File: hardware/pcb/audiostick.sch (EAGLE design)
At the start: 61 parts, among them IC1 TPS73633MBDV, IC3 PCM5102ASW, IC5 AP22804W5, IC6 TINY13V-10SSU, J1 AVRISP6TH127, J2 AUDIO_JACK_3.5MM_PTH, J3 USB-B, T1 BC850

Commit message: Rationalised BOM a little
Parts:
- C14: value 2u2 -> 4u7; device rcl:C-EUC0805 -> rcl:C-EUC0603
- C17: value 1u -> 2u2
- C3: value 10u -> 4u7
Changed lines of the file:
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@@
 <grid distance="0.1" unitdist="inch" unit="inch" style="lines" multiple="1" display="no" altdistance="0.01" altunitdist="inch" altunit="inch"/>
 <layers>
-<layer number="1" name="Top" color="4" fill="1" visible="yes" active="no"/>
-<layer number="16" name="Bottom" color="1" fill="1" visible="yes" active="no"/>
-<layer number="17" name="Pads" color="2" fill="1" visible="yes" active="no"/>
-<layer number="18" name="Vias" color="2" fill="1" visible="yes" active="no"/>
-<layer number="19" name="Unrouted" color="6" fill="1" visible="yes" active="no"/>
-<layer number="20" name="Dimension" color="24" fill="1" visible="yes" active="no"/>
-<layer number="21" name="tPlace" color="7" fill="1" visible="yes" active="no"/>
-<layer number="22" name="bPlace" color="7" fill="1" visible="yes" active="no"/>
-<layer number="23" name="tOrigins" color="15" fill="1" visible="yes" active="no"/>
-<layer number="24" name="bOrigins" color="15" fill="1" visible="yes" active="no"/>
-<layer number="25" name="tNames" color="7" fill="1" visible="yes" active="no"/>
-<layer number="26" name="bNames" color="7" fill="1" visible="yes" active="no"/>
-<layer number="27" name="tValues" color="7" fill="1" visible="yes" active="no"/>
-<layer number="28" name="bValues" color="7" fill="1" visible="yes" active="no"/>
+<layer number="1" name="Top" color="4" fill="1" visible="no" active="no"/>
+<layer number="16" name="Bottom" color="1" fill="1" visible="no" active="no"/>
+<layer number="17" name="Pads" color="2" fill="1" visible="no" active="no"/>
+<layer number="18" name="Vias" color="2" fill="1" visible="no" active="no"/>
+<layer number="19" name="Unrouted" color="6" fill="1" visible="no" active="no"/>
+<layer number="20" name="Dimension" color="24" fill="1" visible="no" active="no"/>
+<layer number="21" name="tPlace" color="7" fill="1" visible="no" active="no"/>
+<layer number="22" name="bPlace" color="7" fill="1" visible="no" active="no"/>
+<layer number="23" name="tOrigins" color="15" fill="1" visible="no" active="no"/>
+<layer number="24" name="bOrigins" color="15" fill="1" visible="no" active="no"/>
+<layer number="25" name="tNames" color="7" fill="1" visible="no" active="no"/>
+<layer number="26" name="bNames" color="7" fill="1" visible="no" active="no"/>
+<layer number="27" name="tValues" color="7" fill="1" visible="no" active="no"/>
+<layer number="28" name="bValues" color="7" fill="1" visible="no" active="no"/>
 <layer number="29" name="tStop" color="7" fill="3" visible="no" active="no"/>
 <layer number="30" name="bStop" color="7" fill="6" visible="no" active="no"/>
@@
 <layer number="35" name="tGlue" color="7" fill="4" visible="no" active="no"/>
 <layer number="36" name="bGlue" color="7" fill="5" visible="no" active="no"/>
-<layer number="37" name="tTest" color="7" fill="1" visible="yes" active="no"/>
-<layer number="38" name="bTest" color="7" fill="1" visible="yes" active="no"/>
+<layer number="37" name="tTest" color="7" fill="1" visible="no" active="no"/>
+<layer number="38" name="bTest" color="7" fill="1" visible="no" active="no"/>
 <layer number="39" name="tKeepout" color="4" fill="11" visible="no" active="no"/>
 <layer number="40" name="bKeepout" color="1" fill="11" visible="no" active="no"/>
@@
 <layer number="44" name="Drills" color="7" fill="1" visible="no" active="no"/>
 <layer number="45" name="Holes" color="7" fill="1" visible="no" active="no"/>
-<layer number="46" name="Milling" color="3" fill="1" visible="yes" active="no"/>
-<layer number="47" name="Measures" color="7" fill="1" visible="yes" active="no"/>
-<layer number="48" name="Document" color="7" fill="1" visible="yes" active="no"/>
-<layer number="49" name="Reference" color="7" fill="1" visible="yes" active="no"/>
-<layer number="50" name="dxf" color="7" fill="1" visible="yes" active="no"/>
-<layer number="51" name="tDocu" color="7" fill="1" visible="yes" active="no"/>
-<layer number="52" name="bDocu" color="7" fill="1" visible="yes" active="no"/>
-<layer number="53" name="tGND_GNDA" color="7" fill="9" visible="yes" active="no"/>
-<layer number="54" name="bGND_GNDA" color="1" fill="9" visible="yes" active="no"/>
-<layer number="56" name="wert" color="7" fill="1" visible="yes" active="no"/>
-<layer number="57" name="tCAD" color="7" fill="1" visible="yes" active="no"/>
-<layer number="59" name="tCarbon" color="7" fill="1" visible="yes" active="no"/>
-<layer number="60" name="bCarbon" color="7" fill="1" visible="yes" active="no"/>
+<layer number="46" name="Milling" color="3" fill="1" visible="no" active="no"/>
+<layer number="47" name="Measures" color="7" fill="1" visible="no" active="no"/>
+<layer number="48" name="Document" color="7" fill="1" visible="no" active="no"/>
+<layer number="49" name="Reference" color="7" fill="1" visible="no" active="no"/>
+<layer number="50" name="dxf" color="7" fill="1" visible="no" active="no"/>
+<layer number="51" name="tDocu" color="7" fill="1" visible="no" active="no"/>
+<layer number="52" name="bDocu" color="7" fill="1" visible="no" active="no"/>
+<layer number="53" name="tGND_GNDA" color="7" fill="9" visible="no" active="no"/>
+<layer number="54" name="bGND_GNDA" color="1" fill="9" visible="no" active="no"/>
+<layer number="56" name="wert" color="7" fill="1" visible="no" active="no"/>
+<layer number="57" name="tCAD" color="7" fill="1" visible="no" active="no"/>
+<layer number="59" name="tCarbon" color="7" fill="1" visible="no" active="no"/>
+<layer number="60" name="bCarbon" color="7" fill="1" visible="no" active="no"/>
 <layer number="88" name="SimResults" color="9" fill="1" visible="yes" active="yes"/>
 <layer number="89" name="SimProbes" color="9" fill="1" visible="yes" active="yes"/>
@@
 <part name="SUPPLY2" library="supply2" library_urn="urn:adsk.eagle:library:372" deviceset="+5V/1" device=""/>
 <part name="IC5" library="AudioStick" deviceset="AP22804" device="W5" package3d_urn="urn:adsk.eagle:package:6644359/2"/>
-<part name="C17" library="rcl" library_urn="urn:adsk.eagle:library:334" deviceset="C-EU" device="C0603" package3d_urn="urn:adsk.eagle:package:23616/2" value="1u"/>
+<part name="C17" library="rcl" library_urn="urn:adsk.eagle:library:334" deviceset="C-EU" device="C0603" package3d_urn="urn:adsk.eagle:package:23616/2" value="2u2"/>
 <part name="C19" library="rcl" library_urn="urn:adsk.eagle:library:334" deviceset="C-EU" device="C0603" package3d_urn="urn:adsk.eagle:package:23616/2" value="100n"/>
 <part name="GND23" library="supply1" library_urn="urn:adsk.eagle:library:371" deviceset="GND" device=""/>
@@
 <part name="D3" library="AudioStick" deviceset="TVS-1" device="" package3d_urn="urn:adsk.eagle:package:23555/3"/>
 <part name="GND31" library="supply1" library_urn="urn:adsk.eagle:library:371" deviceset="GND" device=""/>
-<part name="C14" library="rcl" library_urn="urn:adsk.eagle:library:334" deviceset="C-EU" device="C0805" package3d_urn="urn:adsk.eagle:package:23617/2" value="2u2"/>
+<part name="C14" library="rcl" library_urn="urn:adsk.eagle:library:334" deviceset="C-EU" device="C0603" package3d_urn="urn:adsk.eagle:package:23616/2" value="4u7"/>
 <part name="GND32" library="supply1" library_urn="urn:adsk.eagle:library:371" deviceset="GND" device=""/>
 <part name="GND25" library="supply1" library_urn="urn:adsk.eagle:library:371" deviceset="GND" device=""/>
 <part name="GND14" library="supply1" library_urn="urn:adsk.eagle:library:371" deviceset="GND" device=""/>
 <part name="L3" library="rcl" library_urn="urn:adsk.eagle:library:334" deviceset="R-EU_" device="R0603" package3d_urn="urn:adsk.eagle:package:23555/3" value="F"/>
-<part name="C3" library="rcl" library_urn="urn:adsk.eagle:library:334" deviceset="C-EU" device="C0603" package3d_urn="urn:adsk.eagle:package:23616/2" value="10u"/>
+<part name="C3" library="rcl" library_urn="urn:adsk.eagle:library:334" deviceset="C-EU" device="C0603" package3d_urn="urn:adsk.eagle:package:23616/2" value="4u7"/>
 <part name="IC1" library="AudioStick" deviceset="TPS73633" device="MBDV" package3d_urn="urn:adsk.eagle:package:6644359/2"/>
 <part name="C16" library="rcl" library_urn="urn:adsk.eagle:library:334" deviceset="C-EU" device="C0603" package3d_urn="urn:adsk.eagle:package:23616/2" value="10n"/>

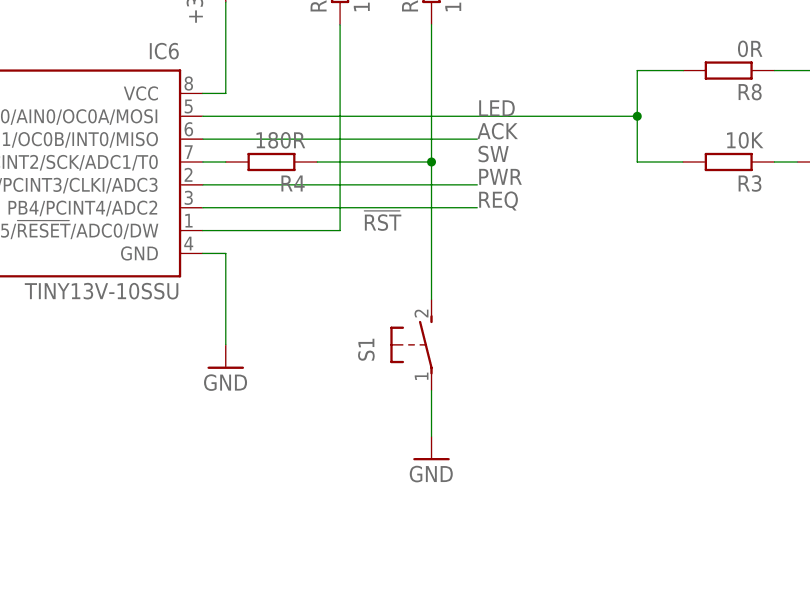
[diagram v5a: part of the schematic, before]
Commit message: Revert to EVQ switch
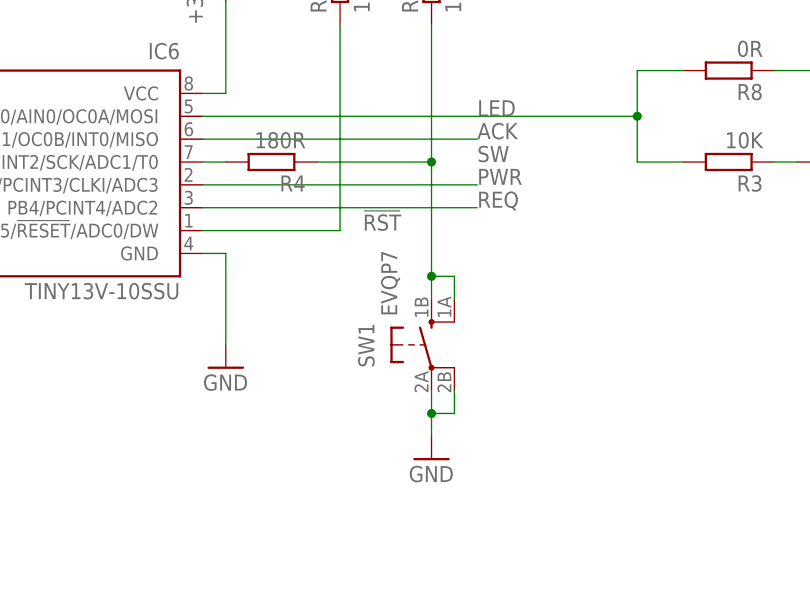
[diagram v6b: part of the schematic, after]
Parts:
- removed S1: (no value), switch-omron:31-XX
- added SW1: EVQP7, AudioStick:EVQP7
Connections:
- net GND: now also SW1.P, SW1.P1; no longer S1.P
- net SW: now also SW1.S, SW1.S1; no longer S1.S
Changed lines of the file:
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@@
 <part name="R4" library="rcl" library_urn="urn:adsk.eagle:library:334" deviceset="R-EU_" device="R0603" package3d_urn="urn:adsk.eagle:package:23555/3" value="180R"/>
 <part name="R8" library="rcl" library_urn="urn:adsk.eagle:library:334" deviceset="R-EU_" device="R0603" package3d_urn="urn:adsk.eagle:package:23555/3" value="0R"/>
-<part name="S1" library="switch-omron" library_urn="urn:adsk.eagle:library:377" deviceset="31-XX" device="" package3d_urn="urn:adsk.eagle:package:27487/1"/>
+<part name="SW1" library="AudioStick" deviceset="EVQP7" device=""/>
 </parts>
 <sheets>
@@
 <attribute name="VALUE" x="120.65" y="356.362" size="1.778" layer="96" rot="R180"/>
 </instance>
-<instance part="S1" gate="1" x="83.82" y="322.58" smashed="yes">
-<attribute name="NAME" x="77.47" y="320.675" size="1.778" layer="95" rot="R90"/>
+<instance part="SW1" gate="G$1" x="83.82" y="322.58" smashed="yes">
+<attribute name="NAME" x="77.47" y="320.04" size="1.778" layer="95" rot="R90"/>
 <attribute name="VALUE" x="80.01" y="325.755" size="1.778" layer="96" rot="R90"/>
 </instance>
@@
 <segment>
 <pinref part="GND1" gate="1" pin="GND"/>
-<wire x1="83.82" y1="312.42" x2="83.82" y2="317.5" width="0.1524" layer="91"/>
-<pinref part="S1" gate="1" pin="P"/>
+<wire x1="83.82" y1="312.42" x2="83.82" y2="314.96" width="0.1524" layer="91"/>
+<pinref part="SW1" gate="G$1" pin="P"/>
+<pinref part="SW1" gate="G$1" pin="P1"/>
+<wire x1="83.82" y1="314.96" x2="83.82" y2="317.5" width="0.1524" layer="91"/>
+<wire x1="83.82" y1="314.96" x2="86.36" y2="314.96" width="0.1524" layer="91"/>
+<wire x1="86.36" y1="314.96" x2="86.36" y2="317.5" width="0.1524" layer="91"/>
+<junction x="83.82" y="314.96"/>
 </segment>
 <segment>
@@
 <segment>
 <pinref part="R9" gate="G$1" pin="1"/>
-<wire x1="83.82" y1="327.66" x2="83.82" y2="342.9" width="0.1524" layer="91"/>
+<wire x1="83.82" y1="327.66" x2="83.82" y2="330.2" width="0.1524" layer="91"/>
+<wire x1="83.82" y1="330.2" x2="83.82" y2="342.9" width="0.1524" layer="91"/>
 <wire x1="83.82" y1="342.9" x2="83.82" y2="358.14" width="0.1524" layer="91"/>
 <label x="88.9" y="342.9" size="1.778" layer="95"/>
@@
 <wire x1="71.12" y1="342.9" x2="83.82" y2="342.9" width="0.1524" layer="91"/>
 <junction x="83.82" y="342.9"/>
-<pinref part="S1" gate="1" pin="S"/>
-</segment>
-<segment>
+<pinref part="SW1" gate="G$1" pin="S"/>
+<pinref part="SW1" gate="G$1" pin="S1"/>
+<wire x1="83.82" y1="330.2" x2="86.36" y2="330.2" width="0.1524" layer="91"/>
+<wire x1="86.36" y1="330.2" x2="86.36" y2="327.66" width="0.1524" layer="91"/>
+<junction x="83.82" y="330.2"/>
+</segment>
+<segment>

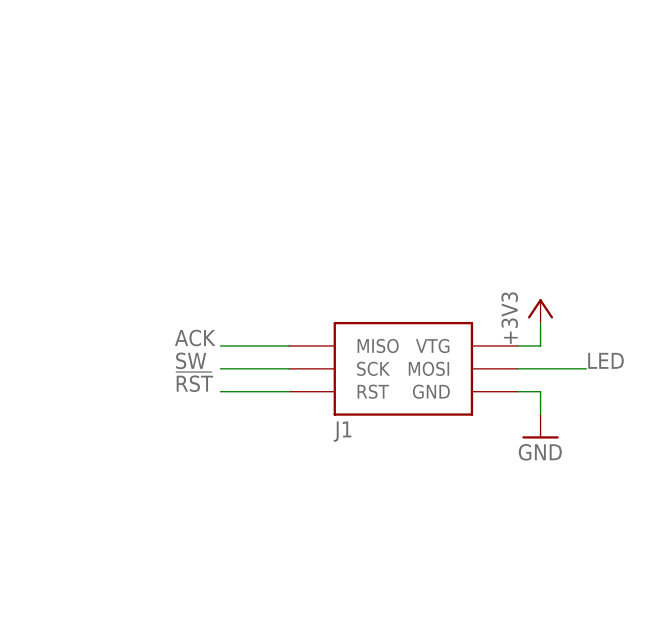
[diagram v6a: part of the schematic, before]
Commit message: Update board, BOM, and firmware
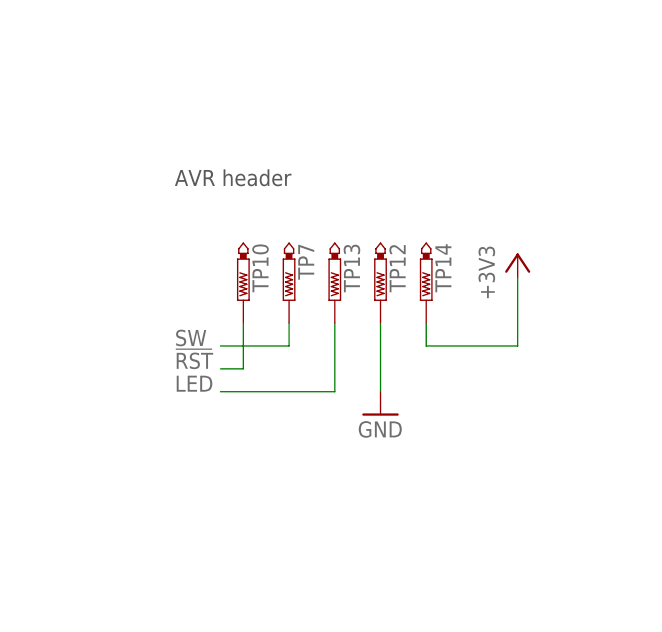
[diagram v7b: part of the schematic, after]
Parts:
- removed J1: AVRISP6TH127, AWJLEagleLib:AVRISP6TH127
- added TP10, TP12, TP13, TP14, TP7: PTR1TP08R, testpad:PTR1TP08R
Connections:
- net !RST: now also TP10.TP; no longer J1.RST
- net +3V3: now also TP14.TP; no longer J1.VTG
- net ACK: no longer J1.MISO
- net GND: now also TP12.TP; no longer J1.GND
- net LED: now also TP13.TP; no longer J1.MOSI
- net SW: now also TP7.TP; no longer J1.SCK
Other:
- note added: "AVR header"
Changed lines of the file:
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@@
 <part name="R13" library="rcl" library_urn="urn:adsk.eagle:library:334" deviceset="R-EU_" device="R0603" package3d_urn="urn:adsk.eagle:package:23555/3" value="10K"/>
 <part name="IC6" library="atmel" library_urn="urn:adsk.eagle:library:105" deviceset="TINY13" device="SSU" package3d_urn="urn:adsk.eagle:package:4358/1" technology="V-10"/>
-<part name="J1" library="AWJLEagleLib" deviceset="AVRISP6" device="TH127"/>
 <part name="+3V5" library="supply1" library_urn="urn:adsk.eagle:library:371" deviceset="+3V3" device=""/>
 <part name="GND19" library="supply1" library_urn="urn:adsk.eagle:library:371" deviceset="GND" device=""/>
@@
 <part name="R8" library="rcl" library_urn="urn:adsk.eagle:library:334" deviceset="R-EU_" device="R0603" package3d_urn="urn:adsk.eagle:package:23555/3" value="0R"/>
 <part name="SW1" library="AudioStick" deviceset="EVQP7" device=""/>
+<part name="TP7" library="testpad" library_urn="urn:adsk.eagle:library:385" deviceset="PTR1" device="TP08R" package3d_urn="urn:adsk.eagle:package:27956/1" value="PTR1TP08R"/>
+<part name="TP10" library="testpad" library_urn="urn:adsk.eagle:library:385" deviceset="PTR1" device="TP08R" package3d_urn="urn:adsk.eagle:package:27956/1" value="PTR1TP08R"/>
+<part name="TP12" library="testpad" library_urn="urn:adsk.eagle:library:385" deviceset="PTR1" device="TP08R" package3d_urn="urn:adsk.eagle:package:27956/1" value="PTR1TP08R"/>
+<part name="TP13" library="testpad" library_urn="urn:adsk.eagle:library:385" deviceset="PTR1" device="TP08R" package3d_urn="urn:adsk.eagle:package:27956/1" value="PTR1TP08R"/>
+<part name="TP14" library="testpad" library_urn="urn:adsk.eagle:library:385" deviceset="PTR1" device="TP08R" package3d_urn="urn:adsk.eagle:package:27956/1" value="PTR1TP08R"/>
 </parts>
 <sheets>
@@
 <text x="119.38" y="96.52" size="1.778" layer="97">ATtiny13 supply</text>
 <text x="134.62" y="358.14" size="1.778" layer="97">Kingbright KPA-3010</text>
+<text x="200.66" y="360.68" size="1.778" layer="97">AVR header</text>
 </plain>
 <instances>
@@
 <attribute name="VALUE" x="55.88" y="327.66" size="1.778" layer="96" rot="MR0"/>
 </instance>
-<instance part="J1" gate="G$1" x="226.06" y="340.36" smashed="yes">
-<attribute name="NAME" x="218.44" y="332.74" size="1.778" layer="95"/>
-</instance>
-<instance part="+3V5" gate="G$1" x="241.3" y="347.98" smashed="yes">
-<attribute name="VALUE" x="238.76" y="342.9" size="1.778" layer="96" rot="R90"/>
-</instance>
-<instance part="GND19" gate="1" x="241.3" y="332.74" smashed="yes">
-<attribute name="VALUE" x="238.76" y="330.2" size="1.778" layer="96"/>
+<instance part="+3V5" gate="G$1" x="238.76" y="353.06" smashed="yes">
+<attribute name="VALUE" x="236.22" y="347.98" size="1.778" layer="96" rot="R90"/>
+</instance>
+<instance part="GND19" gate="1" x="223.52" y="335.28" smashed="yes">
+<attribute name="VALUE" x="220.98" y="332.74" size="1.778" layer="96"/>
 </instance>
 <instance part="TP1" gate="G$1" x="147.32" y="88.9" smashed="yes" rot="R90">
@@
 <attribute name="NAME" x="77.47" y="320.04" size="1.778" layer="95" rot="R90"/>
 <attribute name="VALUE" x="80.01" y="325.755" size="1.778" layer="96" rot="R90"/>
+</instance>
+<instance part="TP7" gate="G$1" x="213.36" y="347.98" smashed="yes" rot="R180">
+<attribute name="NAME" x="214.376" y="354.33" size="1.778" layer="95" rot="R270"/>
+<attribute name="TP_SIGNAL_NAME" x="212.09" y="350.52" size="1.778" layer="97" rot="R180"/>
+</instance>
+<instance part="TP10" gate="G$1" x="208.28" y="347.98" smashed="yes" rot="R180">
+<attribute name="NAME" x="209.296" y="354.33" size="1.778" layer="95" rot="R270"/>
+<attribute name="TP_SIGNAL_NAME" x="207.01" y="350.52" size="1.778" layer="97" rot="R180"/>
+</instance>
+<instance part="TP12" gate="G$1" x="223.52" y="347.98" smashed="yes" rot="R180">
+<attribute name="NAME" x="224.536" y="354.33" size="1.778" layer="95" rot="R270"/>
+<attribute name="TP_SIGNAL_NAME" x="222.25" y="350.52" size="1.778" layer="97" rot="R180"/>
+</instance>
+<instance part="TP13" gate="G$1" x="218.44" y="347.98" smashed="yes" rot="R180">
+<attribute name="NAME" x="219.456" y="354.33" size="1.778" layer="95" rot="R270"/>
+<attribute name="TP_SIGNAL_NAME" x="217.17" y="350.52" size="1.778" layer="97" rot="R180"/>
+</instance>
+<instance part="TP14" gate="G$1" x="228.6" y="347.98" smashed="yes" rot="R180">
+<attribute name="NAME" x="229.616" y="354.33" size="1.778" layer="95" rot="R270"/>
+<attribute name="TP_SIGNAL_NAME" x="227.33" y="350.52" size="1.778" layer="97" rot="R180"/>
 </instance>
 </instances>
@@
 </segment>
 <segment>
-<pinref part="J1" gate="G$1" pin="GND"/>
 <pinref part="GND19" gate="1" pin="GND"/>
-<wire x1="238.76" y1="337.82" x2="241.3" y2="337.82" width="0.1524" layer="91"/>
-<wire x1="241.3" y1="337.82" x2="241.3" y2="335.28" width="0.1524" layer="91"/>
+<pinref part="TP12" gate="G$1" pin="TP"/>
+<wire x1="223.52" y1="337.82" x2="223.52" y2="345.44" width="0.1524" layer="91"/>
 </segment>
 <segment>
@@
 </segment>
 <segment>
-<pinref part="J1" gate="G$1" pin="VTG"/>
 <pinref part="+3V5" gate="G$1" pin="+3V3"/>
-<wire x1="238.76" y1="342.9" x2="241.3" y2="342.9" width="0.1524" layer="91"/>
-<wire x1="241.3" y1="342.9" x2="241.3" y2="345.44" width="0.1524" layer="91"/>
+<wire x1="228.6" y1="342.9" x2="238.76" y2="342.9" width="0.1524" layer="91"/>
+<wire x1="238.76" y1="342.9" x2="238.76" y2="350.52" width="0.1524" layer="91"/>
+<pinref part="TP14" gate="G$1" pin="TP"/>
+<wire x1="228.6" y1="345.44" x2="228.6" y2="342.9" width="0.1524" layer="91"/>
 </segment>
 <segment>
@@
 <net name="!RST" class="0">
 <segment>
-<pinref part="J1" gate="G$1" pin="RST"/>
-<wire x1="213.36" y1="337.82" x2="205.74" y2="337.82" width="0.1524" layer="91"/>
-<label x="200.66" y="337.82" size="1.778" layer="95"/>
+<label x="200.66" y="340.36" size="1.778" layer="95"/>
+<pinref part="TP10" gate="G$1" pin="TP"/>
+<wire x1="208.28" y1="340.36" x2="205.74" y2="340.36" width="0.1524" layer="91"/>
+<wire x1="208.28" y1="345.44" x2="208.28" y2="340.36" width="0.1524" layer="91"/>
 </segment>
 <segment>
@@
 </segment>
 <segment>
-<pinref part="J1" gate="G$1" pin="SCK"/>
-<wire x1="213.36" y1="340.36" x2="205.74" y2="340.36" width="0.1524" layer="91"/>
-<label x="200.66" y="340.36" size="1.778" layer="95"/>
+<label x="200.66" y="342.9" size="1.778" layer="95"/>
+<pinref part="TP7" gate="G$1" pin="TP"/>
+<wire x1="213.36" y1="342.9" x2="205.74" y2="342.9" width="0.1524" layer="91"/>
+<wire x1="213.36" y1="345.44" x2="213.36" y2="342.9" width="0.1524" layer="91"/>
 </segment>
 </net>
@@
 <label x="88.9" y="345.44" size="1.778" layer="95"/>
 <wire x1="58.42" y1="345.44" x2="88.9" y2="345.44" width="0.1524" layer="91"/>
-</segment>
-<segment>
-<pinref part="J1" gate="G$1" pin="MISO"/>
-<wire x1="213.36" y1="342.9" x2="205.74" y2="342.9" width="0.1524" layer="91"/>
-<label x="200.66" y="342.9" size="1.778" layer="95"/>
 </segment>
 <segment>
@@
 </segment>
 <segment>
-<pinref part="J1" gate="G$1" pin="MOSI"/>
-<wire x1="238.76" y1="340.36" x2="246.38" y2="340.36" width="0.1524" layer="91"/>
-<label x="246.38" y="340.36" size="1.778" layer="95"/>
-</segment>
-</net>
+<wire x1="205.74" y1="337.82" x2="218.44" y2="337.82" width="0.1524" layer="91"/>
+<label x="200.66" y="337.82" size="1.778" layer="95"/>
+<pinref part="TP13" gate="G$1" pin="TP"/>
+<wire x1="218.44" y1="337.82" x2="218.44" y2="345.44" width="0.1524" layer="91"/>
+</segment>
+</net>
